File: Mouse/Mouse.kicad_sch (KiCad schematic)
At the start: 17 parts, among them J1B Cable connector (fixed), J2 Controller Plug, SW1 Left, SW2 Right, U1 74HC04, U2 Vertical, U3 Horizontal, U4 74HC04

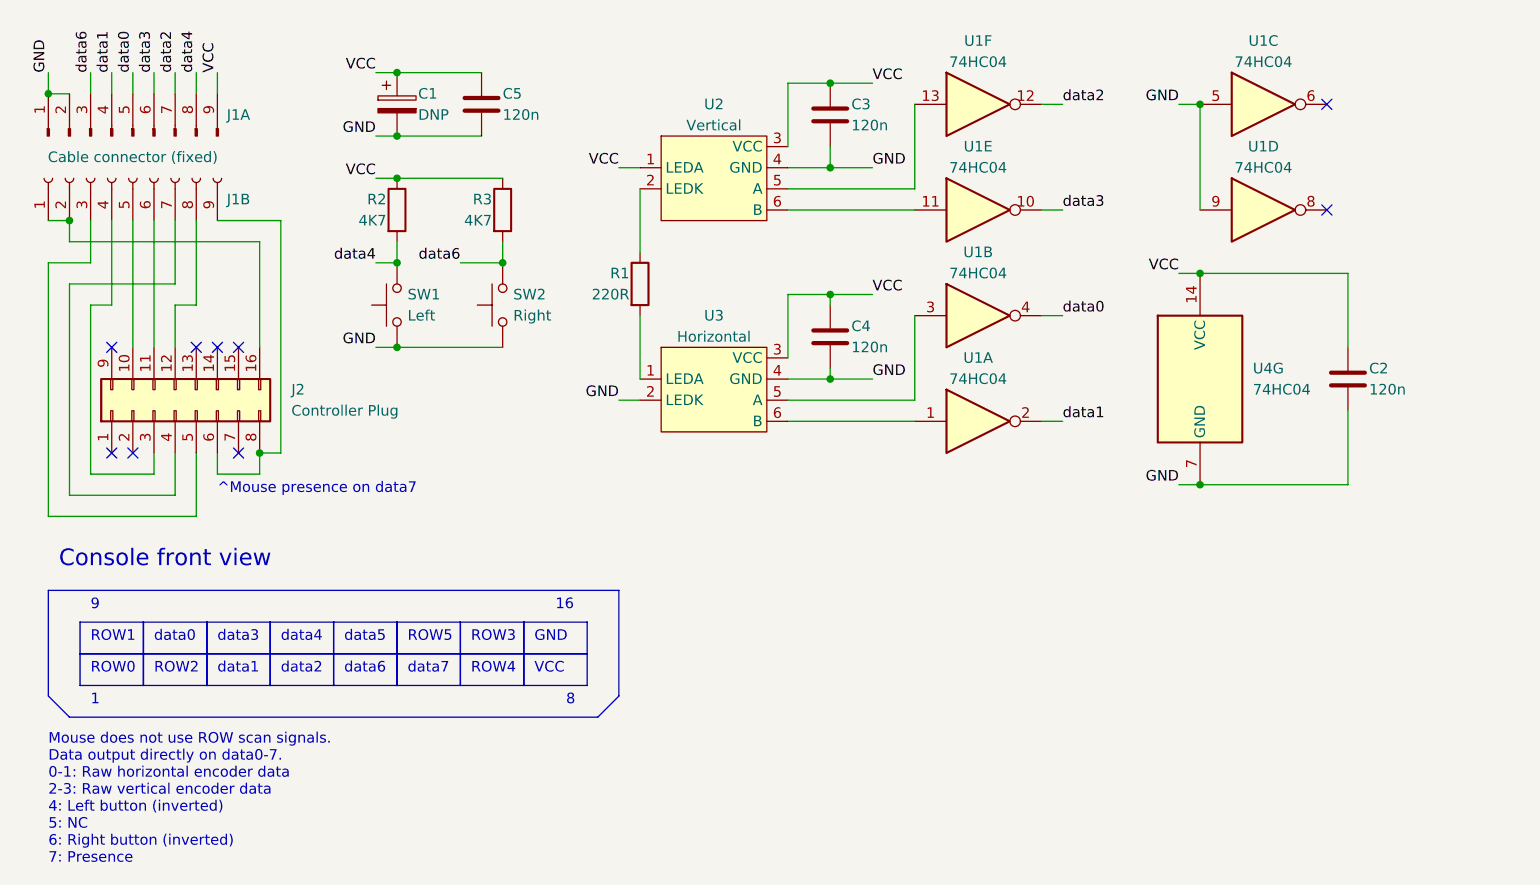
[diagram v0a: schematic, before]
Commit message: Update all to Kicad 9.0 and cleanup
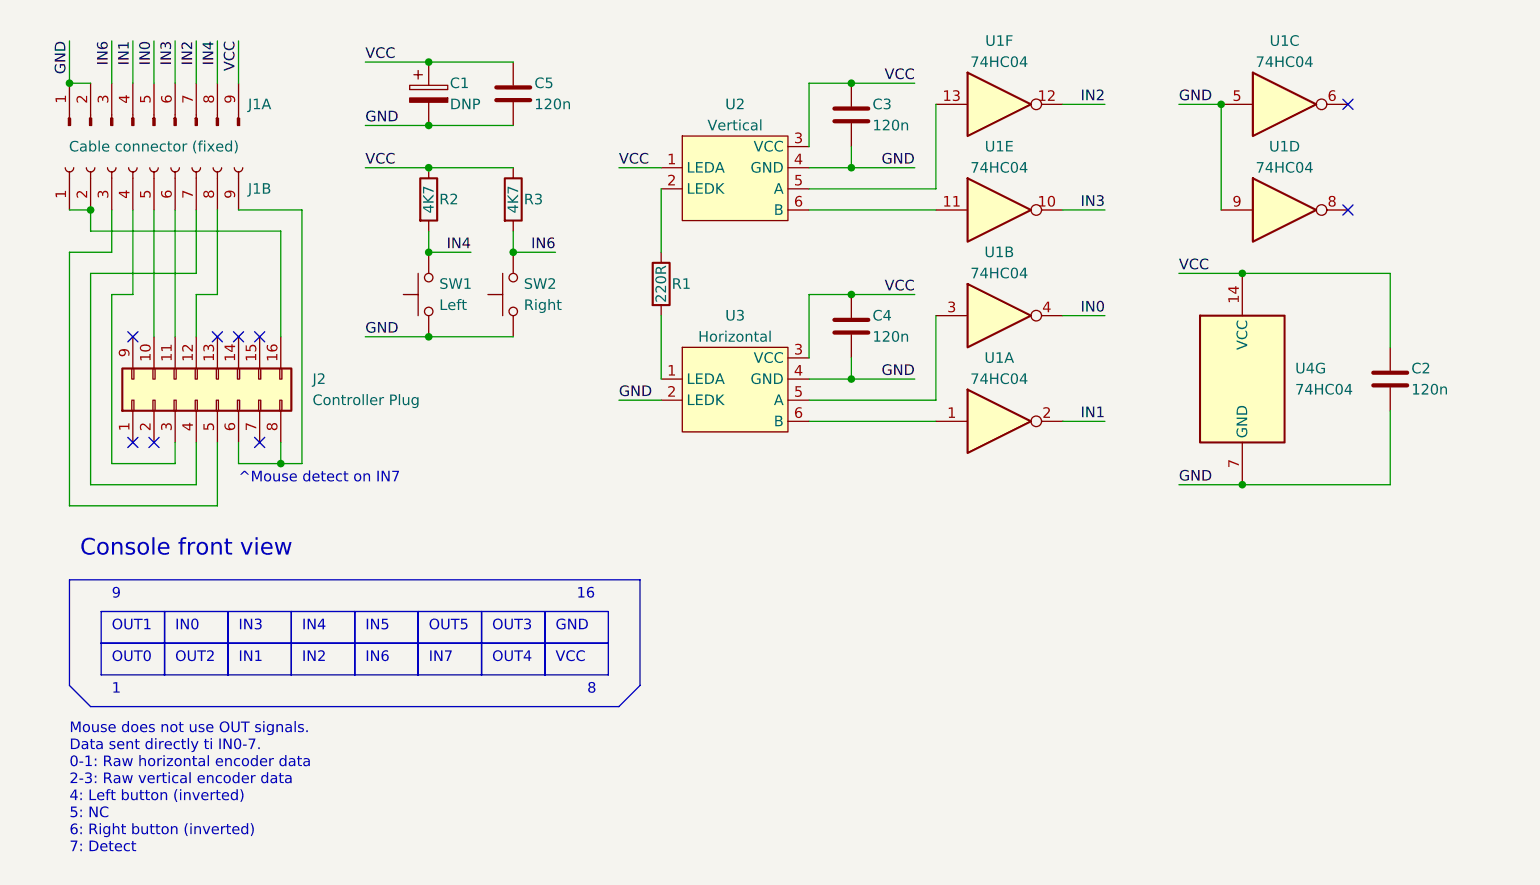
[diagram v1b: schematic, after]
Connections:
- net data0 renamed IN0
- net data1 renamed IN1
- net data2 renamed IN2
- net data3 renamed IN3
- net data4 renamed IN4
- net data6 renamed IN6
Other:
- note added: "IN0"
- note added: "IN1"
- note added: "IN2"
- note added: "IN3"
- note added: "IN4"
- note added: "IN5"
- note added: "IN6"
- note added: "IN7"
- note added: "Mouse does not use OUT signals. Data sent directly ti IN0-7. 0-1: Raw horizontal encoder data 2-3: Raw vertical encoder data 4: Left button (inverted) 5: NC 6: Right button (inverted) 7: Detect"
- note added: "OUT0"
- note added: "OUT1"
- note added: "OUT2"
- note added: "OUT3"
- note added: "OUT4"
- note added: "OUT5"
- note added: "^Mouse detect on IN7"
- note removed: "Mouse does not use ROW scan signals. Data output directly on data0-7. 0-1: Raw horizontal encoder data 2-3: Raw vertical encoder data 4: Left button (inverted) 5: NC 6: Right button (inverted) 7: Presence"
- note removed: "ROW0"
- note removed: "ROW1"
- note removed: "ROW2"
- note removed: "ROW3"
- note removed: "ROW4"
- note removed: "ROW5"
- note removed: "^Mouse presence on data7"
- note removed: "data0"
- note removed: "data1"
- note removed: "data2"
- note removed: "data3"
- note removed: "data4"
- note removed: "data5"
- note removed: "data6"
- note removed: "data7"
- moved on the sheet: C1, C2, C3, C4, C5, J1A, J1B, J2, R1, R2, R3, SW1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

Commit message: Unify project part libs
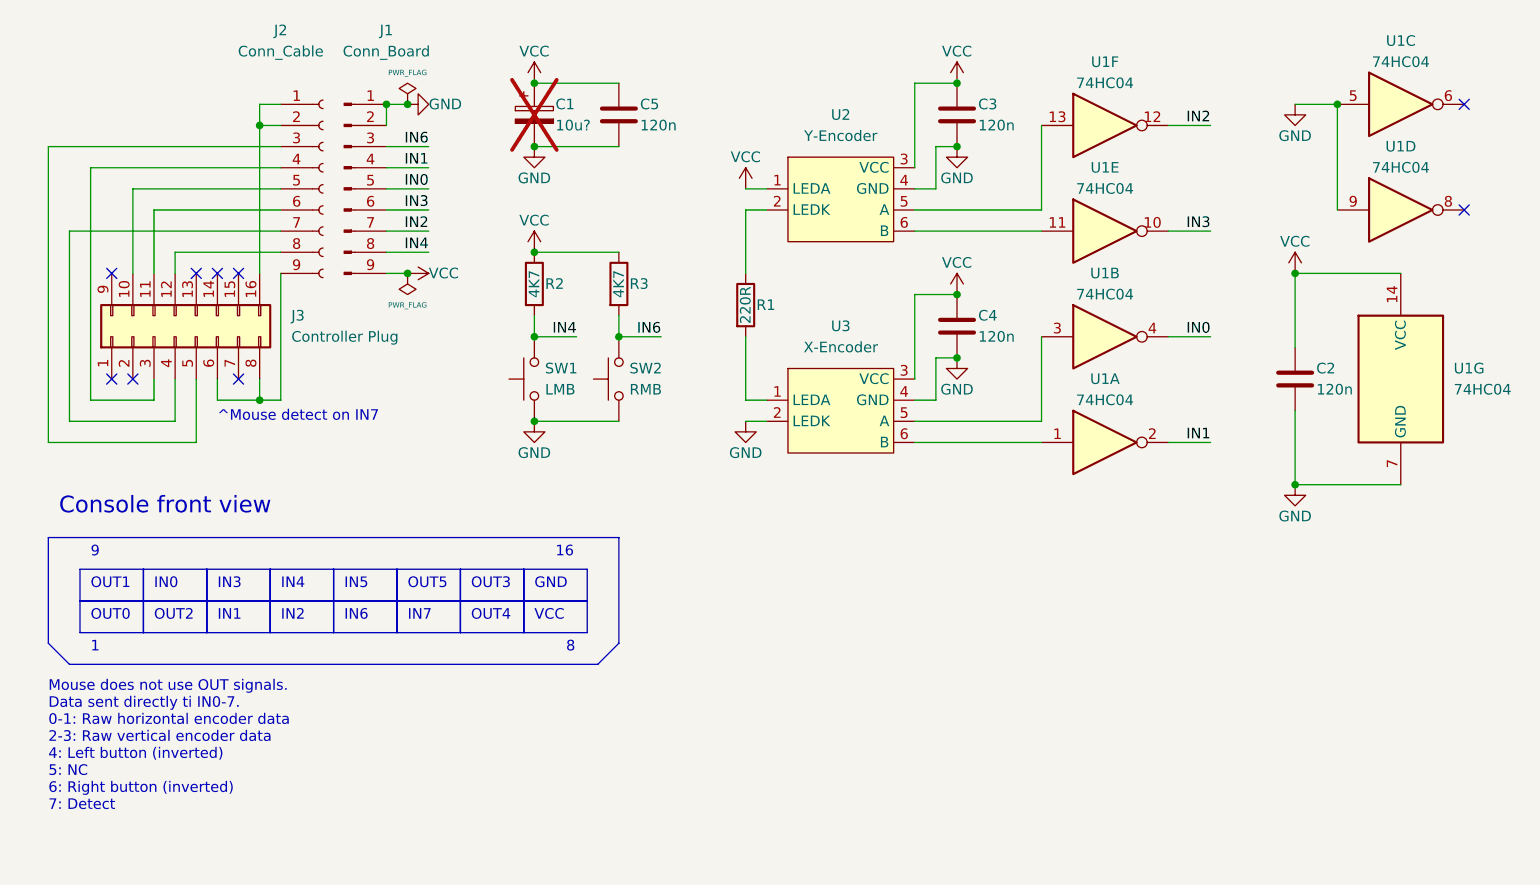
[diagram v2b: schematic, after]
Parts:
- C1: value DNP -> 10u?; now not fitted; now left out of the parts list
- J1: renamed from J1A; value ~ -> Conn_Board
- J2: renamed from J1B; value Cable connector (fixed) -> Conn_Cable
- SW1: value Left -> LMB
- SW2: value Right -> RMB
- U2: value Vertical -> Y-Encoder; symbol MouseParts:Encoder -> loopy-parts:RotaryEncoder_Optical
- U3: value Horizontal -> X-Encoder; symbol MouseParts:Encoder -> loopy-parts:RotaryEncoder_Optical
- renumbered J2 to J3, U4 to U1
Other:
- moved on the sheet: C2, C3, C4, C5, J1, J2, J3, R1, R2, R3, SW1, SW2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
